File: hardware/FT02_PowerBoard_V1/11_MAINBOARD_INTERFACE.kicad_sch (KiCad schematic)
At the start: 0 parts

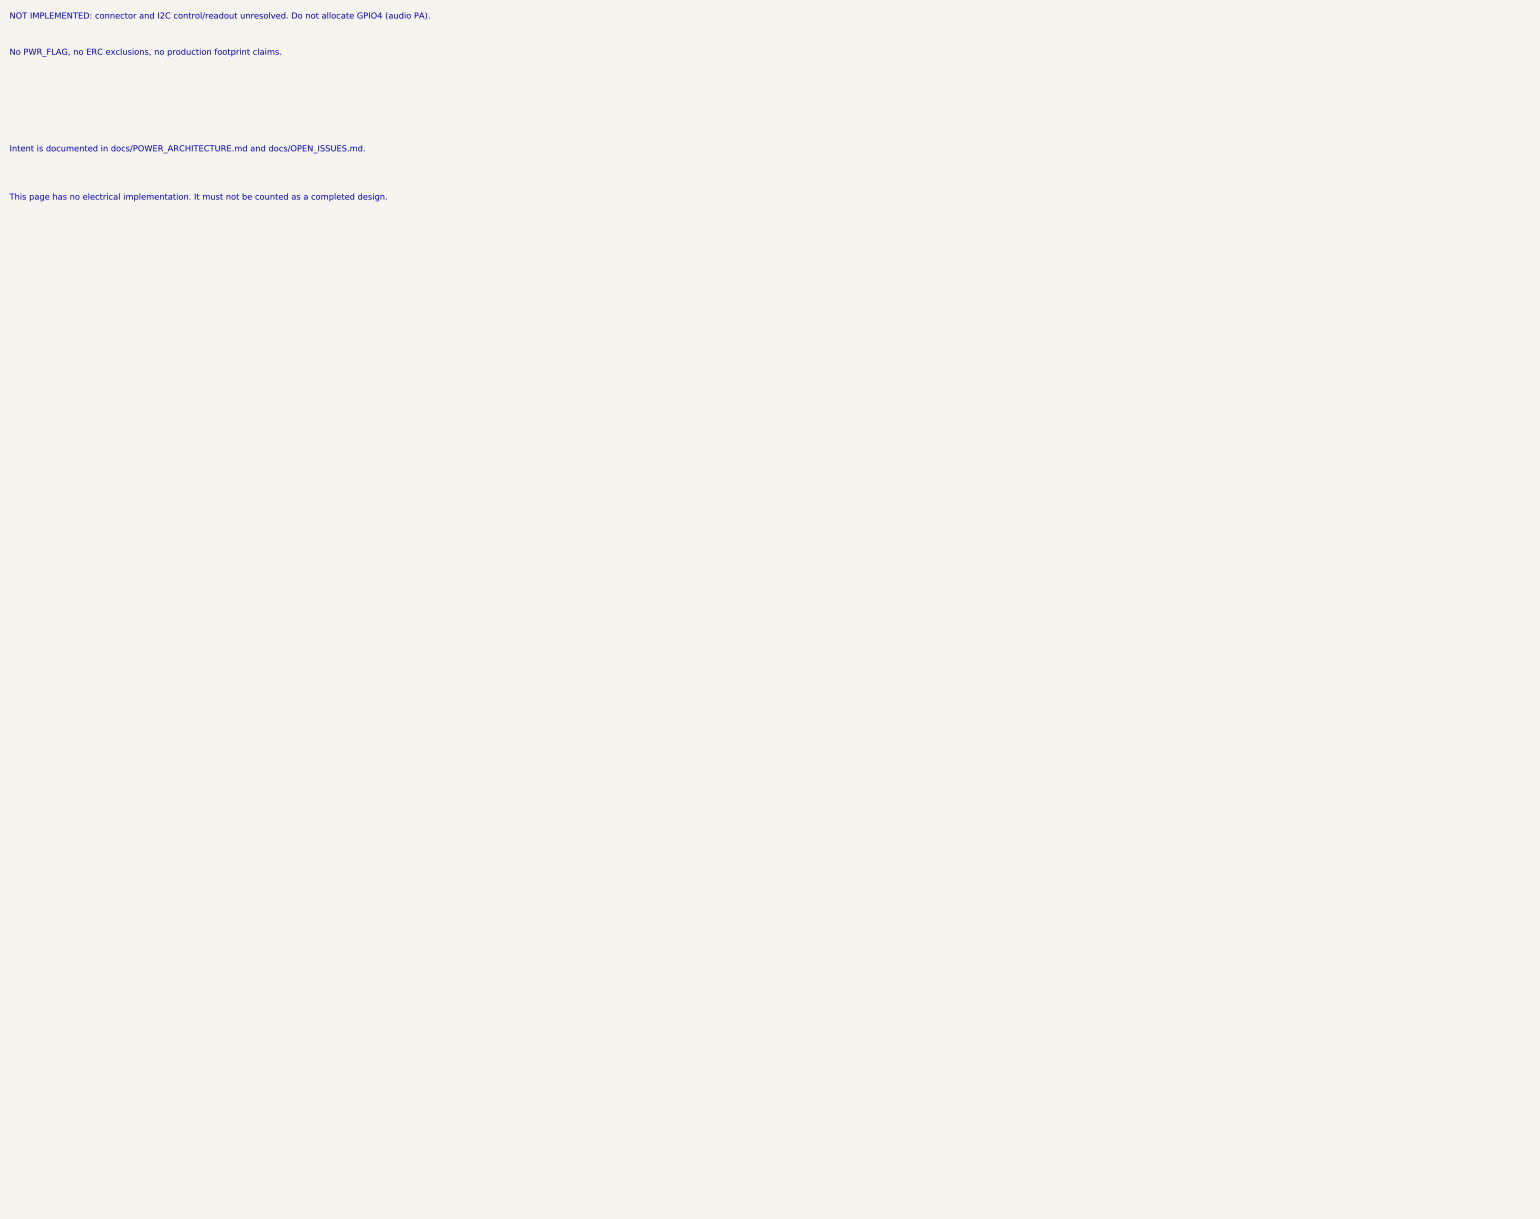
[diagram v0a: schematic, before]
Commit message: Wire FT02 Phase 1 power stages and verify partial shunt boundary
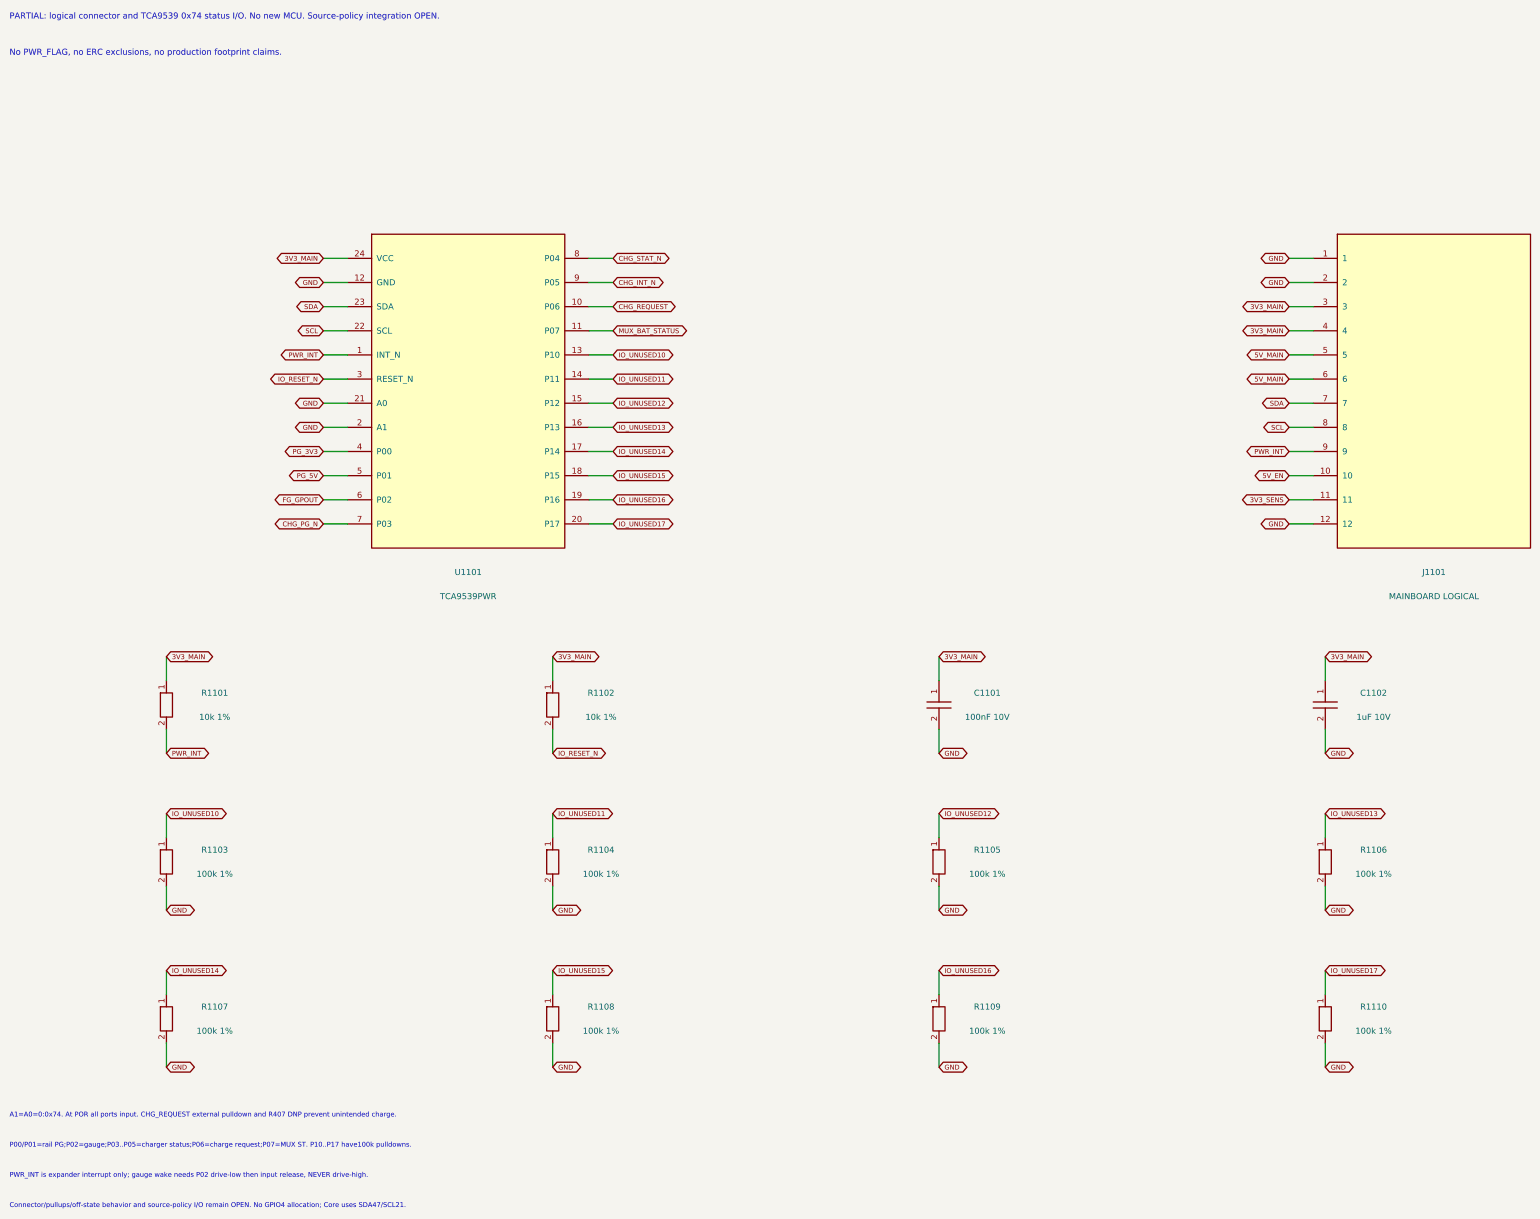
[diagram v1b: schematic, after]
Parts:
- added C1101: 100nF 10V, symbol FT02_Reference:C
- added C1102: 1uF 10V, symbol FT02_Reference:C
- added J1101: MAINBOARD LOGICAL, symbol FT02_Reference:CONN12
- added R1101, R1102: 10k 1%, symbol FT02_Reference:R
- added R1103, R1104, R1105, R1106, R1107, R1108, R1109, R1110: 100k 1%, symbol FT02_Reference:R
- added U1101: TCA9539PWR, symbol FT02_Reference:TCA9539PW
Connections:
- new net 3V3_MAIN: C1101.1, C1102.1, J1101.3, J1101.4, R1101.1, R1102.1, U1101.24 (VCC)
- new net 3V3_SENS: J1101.11
- new net 5V_EN: J1101.10
- new net 5V_MAIN: J1101.5, J1101.6
- new net CHG_INT_N: U1101.9 (P05)
- new net CHG_PG_N: U1101.7 (P03)
- new net CHG_REQUEST: U1101.10 (P06)
- new net CHG_STAT_N: U1101.8 (P04)
- new net FG_GPOUT: U1101.6 (P02)
- new net GND: C1101.2, C1102.2, J1101.1, J1101.12, J1101.2, R1103.2, R1104.2, R1105.2, R1106.2, R1107.2, R1108.2, R1109.2, R1110.2, U1101.12 (GND), U1101.2 (A1), U1101.21 (A0)
- new net IO_RESET_N: R1102.2, U1101.3 (RESET_N)
- new net IO_UNUSED10: R1103.1, U1101.13 (P10)
- new net IO_UNUSED11: R1104.1, U1101.14 (P11)
- new net IO_UNUSED12: R1105.1, U1101.15 (P12)
- new net IO_UNUSED13: R1106.1, U1101.16 (P13)
- new net IO_UNUSED14: R1107.1, U1101.17 (P14)
- new net IO_UNUSED15: R1108.1, U1101.18 (P15)
- new net IO_UNUSED16: R1109.1, U1101.19 (P16)
- new net IO_UNUSED17: R1110.1, U1101.20 (P17)
- new net MUX_BAT_STATUS: U1101.11 (P07)
- new net PG_3V3: U1101.4 (P00)
- new net PG_5V: U1101.5 (P01)
- new net PWR_INT: J1101.9, R1101.2, U1101.1 (INT_N)
- new net SCL: J1101.8, U1101.22 (SCL)
- new net SDA: J1101.7, U1101.23 (SDA)
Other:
- note added: "A1=A0=0:0x74. At POR all ports input. CHG_REQUEST external pulldown and R407 DNP prevent unintended charge."
- note added: "Connector/pullups/off-state behavior and source-policy I/O remain OPEN. No GPIO4 allocation; Core uses SDA47/SCL21."
- note added: "P00/P01=rail PG;P02=gauge;P03..P05=charger status;P06=charge request;P07=MUX ST. P10..P17 have100k pulldowns."
- note added: "PARTIAL: logical connector and TCA9539 0x74 status I/O. No new MCU. Source-policy integration OPEN."
- note added: "PWR_INT is expander interrupt only; gauge wake needs P02 drive-low then input release, NEVER drive-high."
- note removed: "Intent is documented in docs/POWER_ARCHITECTURE.md and docs/OPEN_ISSUES.md."
- note removed: "NOT IMPLEMENTED: connector and I2C control/readout unresolved. Do not allocate GPIO4 (audio PA)."
- note removed: "This page has no electrical implementation. It must not be counted as a completed design."
